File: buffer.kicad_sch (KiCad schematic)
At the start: 1 part, among them U3 OPA1622

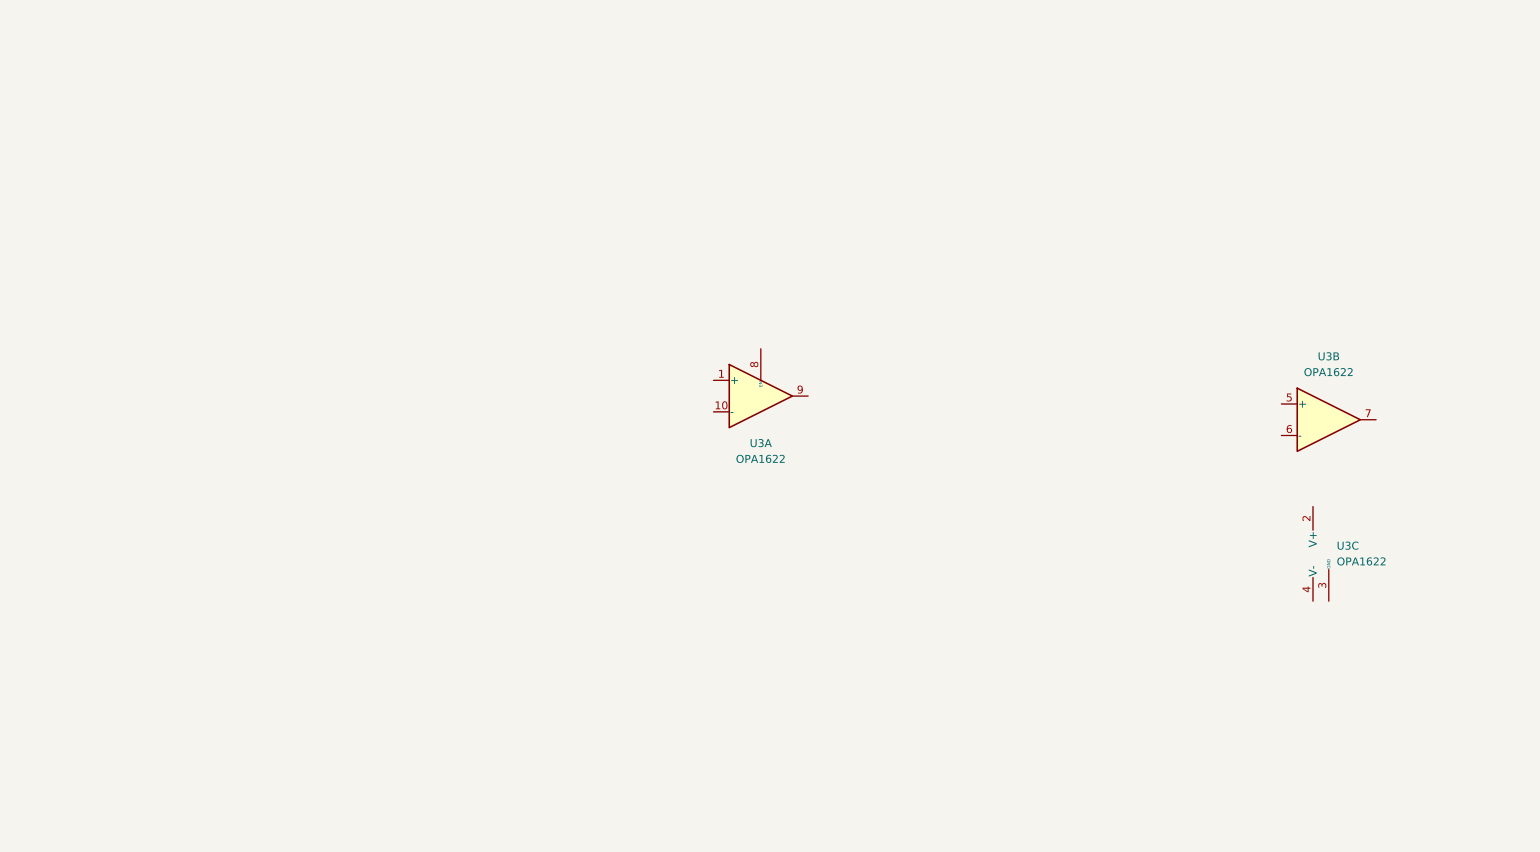
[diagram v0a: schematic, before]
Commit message: Implemented boost stage and now working on schematics for current buffers and rail splitter.
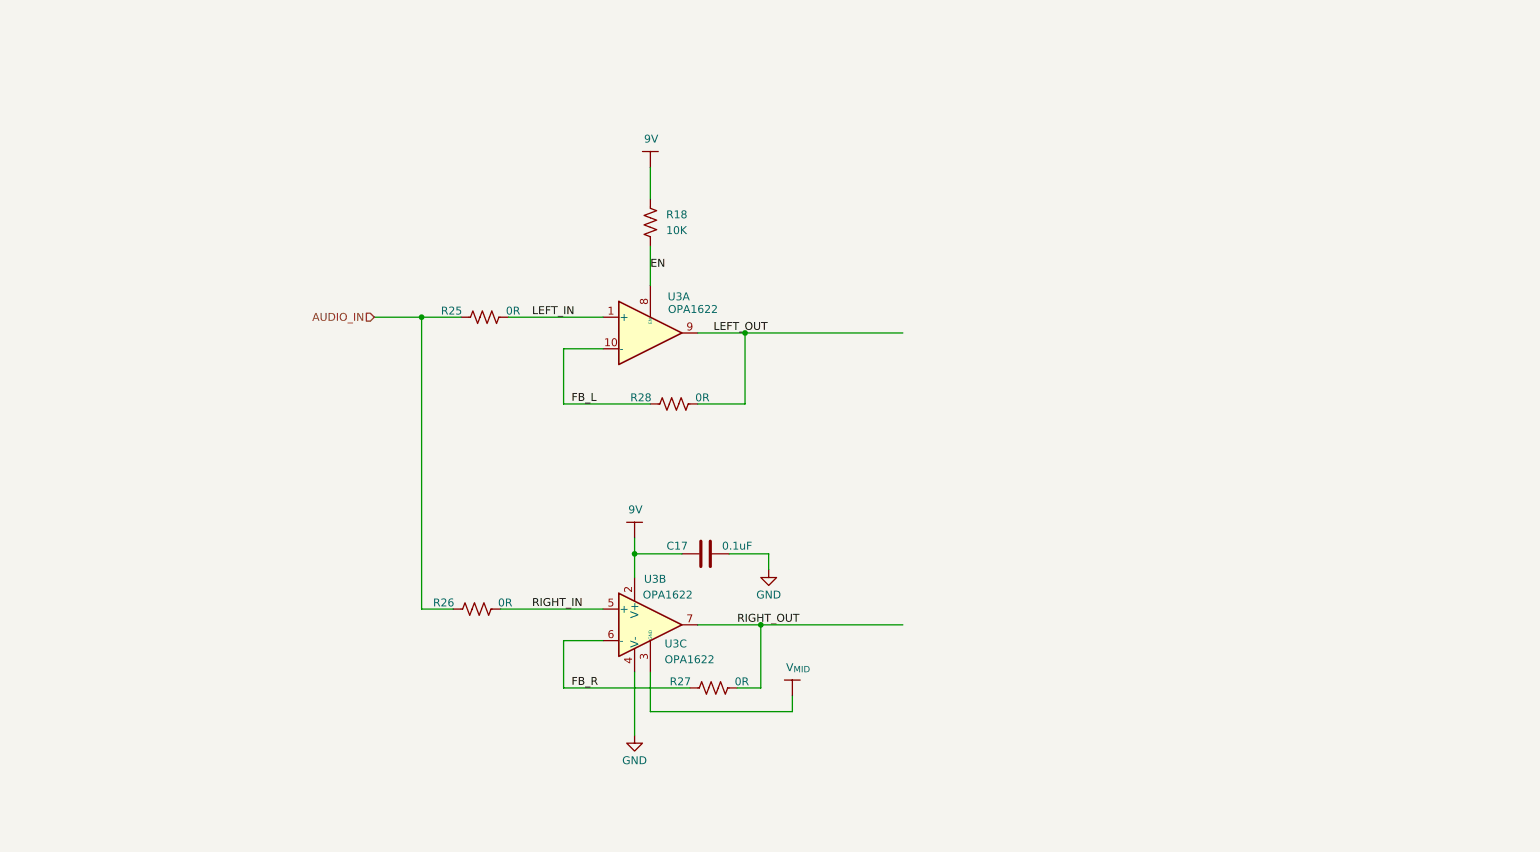
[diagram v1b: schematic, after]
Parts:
- added C17: 0.1uF, Capacitor_SMD:C_0402_1005Metric, symbol #inventree_kicad:C_0U1_X7R_16V_0402
- added R18: 10K, Resistor_SMD:R_0402_1005Metric, symbol #inventree_kicad:R_10K_0402_1PCT_0W0625
- added R25, R26, R27, R28: 0R, symbol Device:R_US
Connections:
- net GND: now reaches U3.11 (V-), U3.4 (V-)
- net GND: now also C17.2
- net 9V: now reaches U3.2 (V+)
- net 9V: now also C17.1, R18.1
- net V_{MID}: now reaches U3.3 (GND)
- net LEFT_IN: now reaches U3.1 (+)
- net LEFT_IN: now also R25.2
- net FB_L: now reaches U3.10 (-)
- net FB_L: now also R28.1
- net EN: now reaches U3.8 (EN)
- net EN: now also R18.2
- net LEFT_OUT: now reaches U3.9
- net LEFT_OUT: now also R28.2
- net RIGHT_IN: now reaches U3.5 (+)
- net RIGHT_IN: now also R26.2
- net FB_R: now reaches U3.6 (-)
- net FB_R: now also R27.1
- net RIGHT_OUT: now reaches U3.7
- net RIGHT_OUT: now also R27.2
- new net AUDIO_IN: R25.1, R26.1
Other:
- title: (none) -> ${PROJECT_NAME}
- moved on the sheet: U3A, U3B, U3C

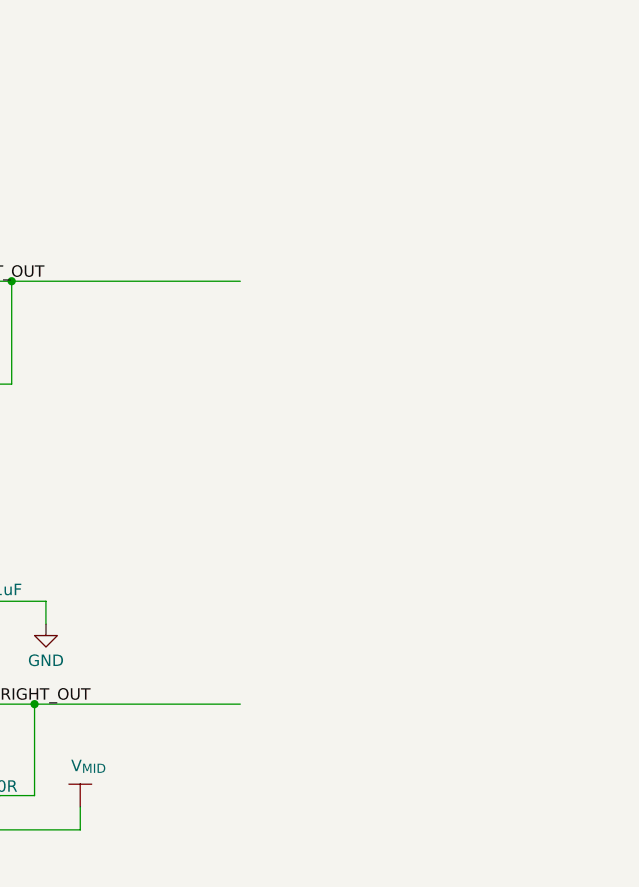
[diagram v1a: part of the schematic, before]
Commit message: Started working on watchdog circuit.
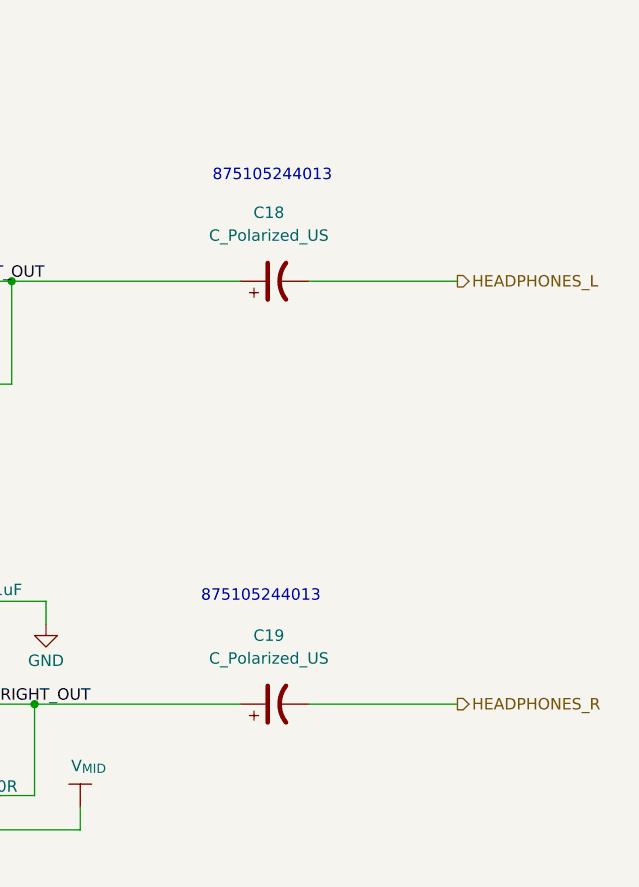
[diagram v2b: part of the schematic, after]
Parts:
- added C18, C19: C_Polarized_US, symbol Device:C_Polarized_US
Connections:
- net LEFT_OUT: now also C18.1
- net RIGHT_OUT: now also C19.1
- new net HEADPHONES_L: C18.2
- new net HEADPHONES_R: C19.2
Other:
- note added: "875105244013"
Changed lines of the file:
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@@
 		(comment 1 "${PCBA_IPN}")
+	)
+	(text "875105244013"
+		(exclude_from_sim no)
+		(at 166.116 67.056 0)
+		(effects
+			(font
+				(size 1.27 1.27)
+			)
+		)
+	)
+	(text "875105244013"
+		(exclude_from_sim no)
+		(at 164.846 113.792 0)
+		(effects
+			(font
+				(size 1.27 1.27)
+			)
+		)
 	)
 	(junction
@@
 	(wire
 		(pts
+			(xy 170.18 78.74) (xy 186.69 78.74)
+		)
+		(stroke
+			(width 0)
+			(type default)
+		)
+	)
+	(wire
+		(pts
 			(xy 107.95 90.17) (xy 121.92 90.17)
 		)
@@
 		(pts
 			(xy 129.54 78.74) (xy 137.16 78.74)
+		)
+		(stroke
+			(width 0)
+			(type default)
+		)
+	)
+	(wire
+		(pts
+			(xy 170.18 125.73) (xy 186.69 125.73)
 		)
 		(stroke
@@
 			)
 			(justify left bottom)
+		)
+	)
+	(hierarchical_label "HEADPHONES_L"
+		(shape output)
+		(at 186.69 78.74 0)
+		(effects
+			(font
+				(size 1.27 1.27)
+			)
+			(justify left)
+		)
+	)
+	(hierarchical_label "HEADPHONES_R"
+		(shape output)
+		(at 186.69 125.73 0)
+		(effects
+			(font
+				(size 1.27 1.27)
+			)
+			(justify left)
 		)
 	)
@@
 	)
 	(symbol
+		(lib_id "Device:C_Polarized_US")
+		(at 166.37 78.74 90)
+		(unit 1)
+		(body_style 1)
+		(exclude_from_sim no)
+		(in_bom yes)
+		(on_board yes)
+		(in_pos_files yes)
+		(dnp no)
+		(fields_autoplaced yes)
+		(property "Reference" "C18"
+			(at 165.735 71.12 90)
+			(show_name no)
+			(do_not_autoplace no)
+			(effects
+				(font
+					(size 1.27 1.27)
+				)
+			)
+		)
+		(property "Value" "C_Polarized_US"
+			(at 165.735 73.66 90)
+			(show_name no)
+			(do_not_autoplace no)
+			(effects
+				(font
+					(size 1.27 1.27)
+				)
+			)
+		)
+		(property "Footprint" ""
+			(at 166.37 78.74 0)
+			(hide yes)
+			(show_name no)
+			(do_not_autoplace no)
+			(effects
+				(font
+					(size 1.27 1.27)
+				)
+			)
+		)
+		(property "Datasheet" ""
+			(at 166.37 78.74 0)
+			(hide yes)
+			(show_name no)
+			(do_not_autoplace no)
+			(effects
+				(font
+					(size 1.27 1.27)
+				)
+			)
+		)
+		(property "Description" "Polarized capacitor, US symbol"
+			(at 166.37 78.74 0)
+			(hide yes)
+			(show_name no)
+			(do_not_autoplace no)
+			(effects
+				(font
+					(size 1.27 1.27)
+				)
+			)
+		)
+		(pin "1"
+		)
+		(pin "2"
+		)
+		(instances
+			(project "headphone_amp"
+				(path "/62ffec33-ae93-49a8-bfe6-566578dd8e82/8fba3b35-d615-47af-8081-02211a3ffbd2"
+					(reference "C18")
+					(unit 1)
+				)
+			)
+		)
+	)
+	(symbol
 		(lib_id "Device:R_US")
 		(at 93.98 123.19 90)
@@
 					(unit 1)
 				)
+			)
+		)
+	)
+	(symbol
+		(lib_id "Device:C_Polarized_US")
+		(at 166.37 125.73 90)
+		(unit 1)
+		(body_style 1)
+		(exclude_from_sim no)
+		(in_bom yes)
+		(on_board yes)
+		(in_pos_files yes)
+		(dnp no)
+		(fields_autoplaced yes)
+		(property "Reference" "C19"
+			(at 165.735 118.11 90)
+			(show_name no)
+			(do_not_autoplace no)
+			(effects
+				(font
+					(size 1.27 1.27)
+				)
+			)
+		)
+		(property "Value" "C_Polarized_US"
+			(at 165.735 120.65 90)
+			(show_name no)
+			(do_not_autoplace no)
+			(effects
+				(font
+					(size 1.27 1.27)
+				)
+			)
+		)
+		(property "Footprint" ""
+			(at 166.37 125.73 0)
+			(hide yes)
+			(show_name no)
+			(do_not_autoplace no)
+			(effects
+				(font
+					(size 1.27 1.27)
+				)
+			)
+		)
+		(property "Datasheet" ""
+			(at 166.37 125.73 0)
+			(hide yes)
+			(show_name no)
+			(do_not_autoplace no)
+			(effects
+				(font
+					(size 1.27 1.27)
+				)
+			)
+		)
+		(property "Description" "Polarized capacitor, US symbol"
+			(at 166.37 125.73 0)
+			(hide yes)
+			(show_name no)
+			(do_not_autoplace no)
+			(effects
+				(font
+					(size 1.27 1.27)
+				)
+			)
+		)
+		(pin "1"
+		)
+		(pin "2"
+		)
+		(instances
+			(project "headphone_amp"
+				(path "/62ffec33-ae93-49a8-bfe6-566578dd8e82/8fba3b35-d615-47af-8081-02211a3ffbd2"
+					(reference "C19")
+					(unit 1)
+				)

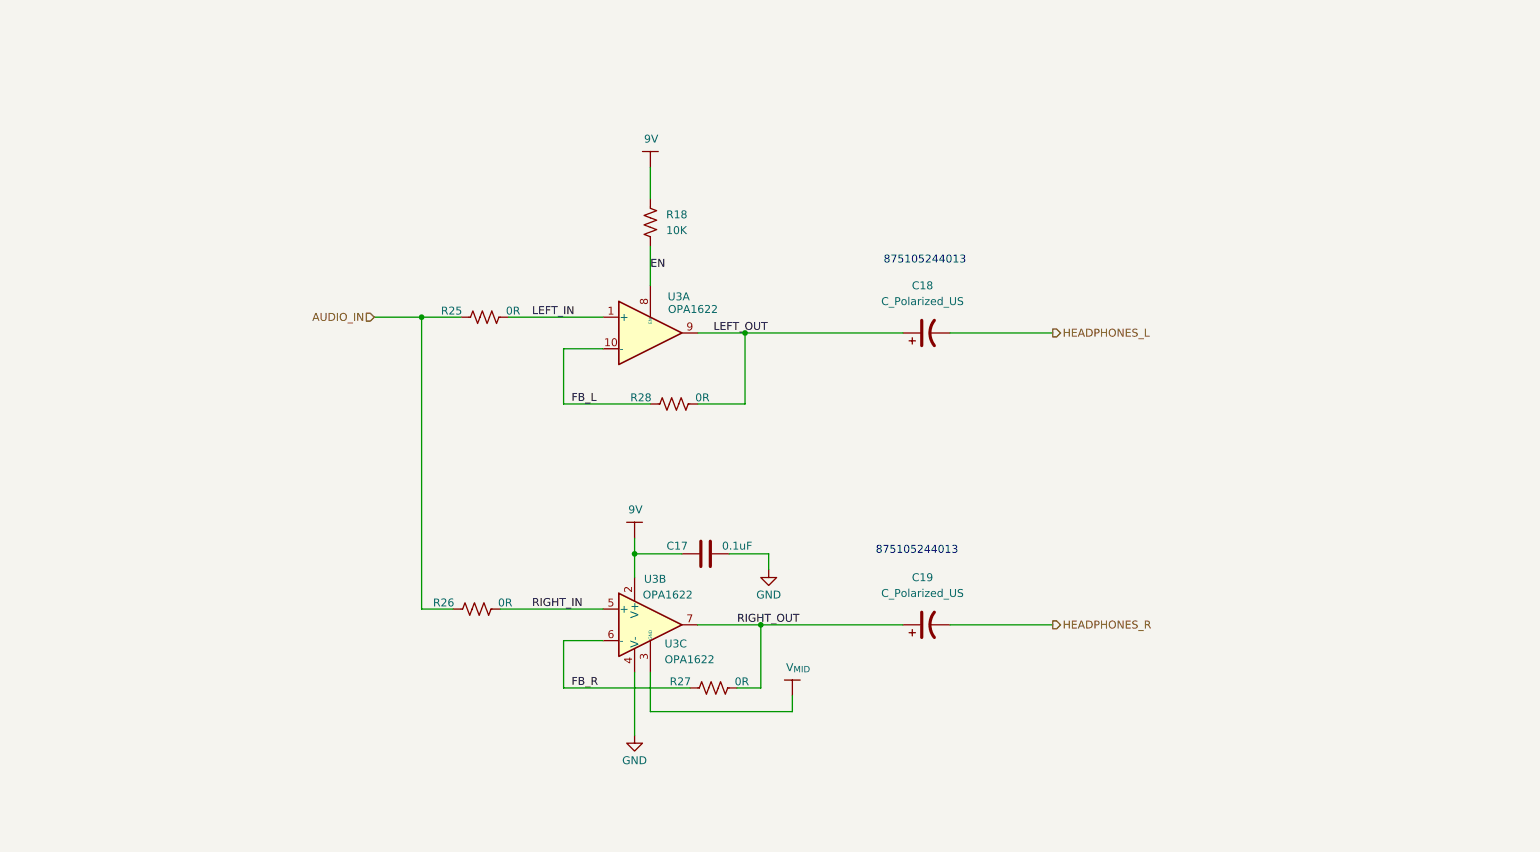
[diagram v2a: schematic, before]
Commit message: First rough draft of schematics complete -- missing a lot of PLM/Inventree work. Ran through several Claude reviews.
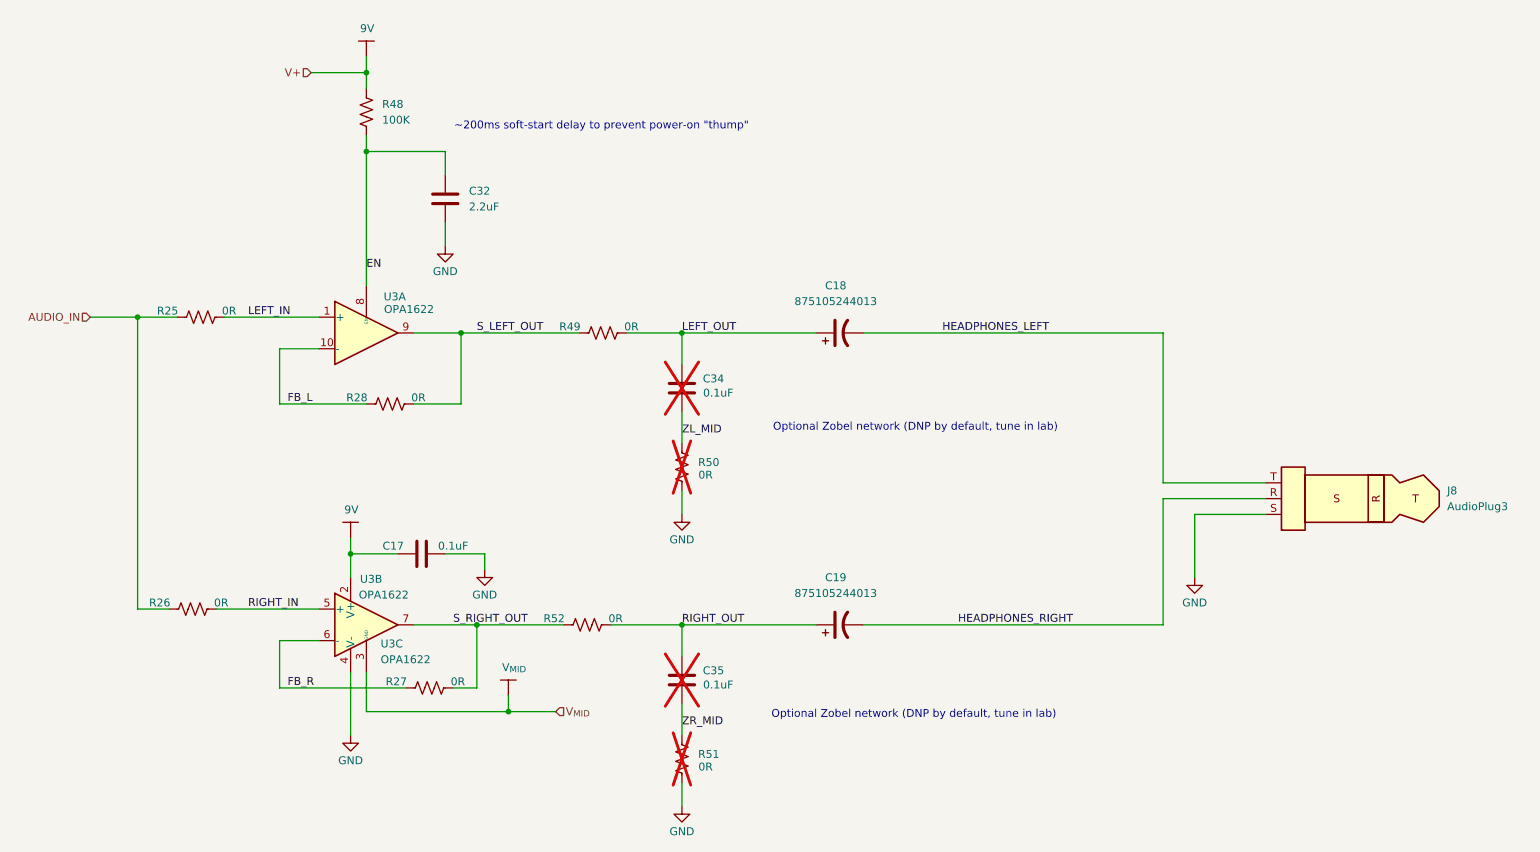
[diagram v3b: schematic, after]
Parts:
- removed R18: 10K, Resistor_SMD:R_0402_1005Metric, symbol #inventree_kicad:R_10K_0402_1PCT_0W0625
- added C32: 2.2uF, symbol Device:C
- added C34, C35: 0.1uF, Capacitor_SMD:C_0402_1005Metric, symbol #inventree_kicad:C_0U1_X7R_16V_0402
- added J8: AudioPlug3, Connector_Audio:Jack_3.5mm_CUI_SJ-3523-SMT_Horizontal, symbol Connector_Audio:AudioPlug3
- added R48: 100K, Resistor_SMD:R_0402_1005Metric, symbol #inventree_kicad:R_100K_0402_1PCT_0W0625
- added R49, R50, R51, R52: 0R, symbol Device:R_US
- C18, C19: value C_Polarized_US -> 875105244013
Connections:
- net 9V: now also R48.2
- net EN: now also C32.2, R48.1
- net GND: now also C32.1, J8.S, R50.1, R51.1
- net LEFT_OUT: now also C34.2, R49.2; no longer R28.2, U3.9
- net RIGHT_OUT: now also C35.2, R52.2; no longer R27.2, U3.7
- net HEADPHONES_L renamed HEADPHONES_LEFT
- net HEADPHONES_LEFT: now also J8.T
- net HEADPHONES_R renamed HEADPHONES_RIGHT
- net HEADPHONES_RIGHT: now also J8.R
- new net S_LEFT_OUT: R28.2, R49.1, U3.9
- new net S_RIGHT_OUT: R27.2, R52.1, U3.7
- new net ZL_MID: C34.1, R50.2
- new net ZR_MID: C35.1, R51.2
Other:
- note added: "Optional Zobel network (DNP by default, tune in lab)"
- note added: "~200ms soft-start delay to prevent power-on "thump""
- note removed: "875105244013"
- moved on the sheet: C17, C18, C19, R25, R26, R27, R28, U3A, U3B, U3C
